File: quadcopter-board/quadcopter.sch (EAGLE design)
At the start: 75 parts, among them J2 AVR_SPI_PRG_6NS, SW1 PUSHBUTTON_SMD-VERTICAL-1, U2 ATMEGA128RFA1

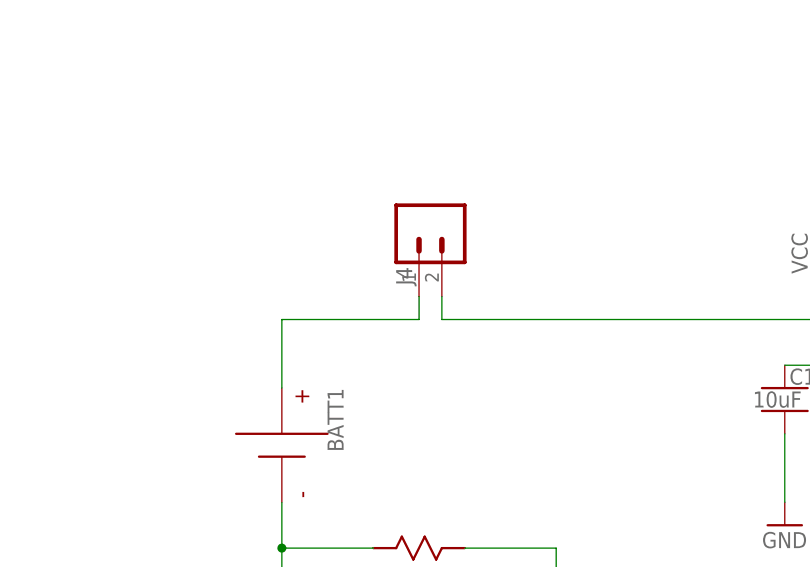
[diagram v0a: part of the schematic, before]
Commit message: Applied update to library and dru files. Passing DFM testing
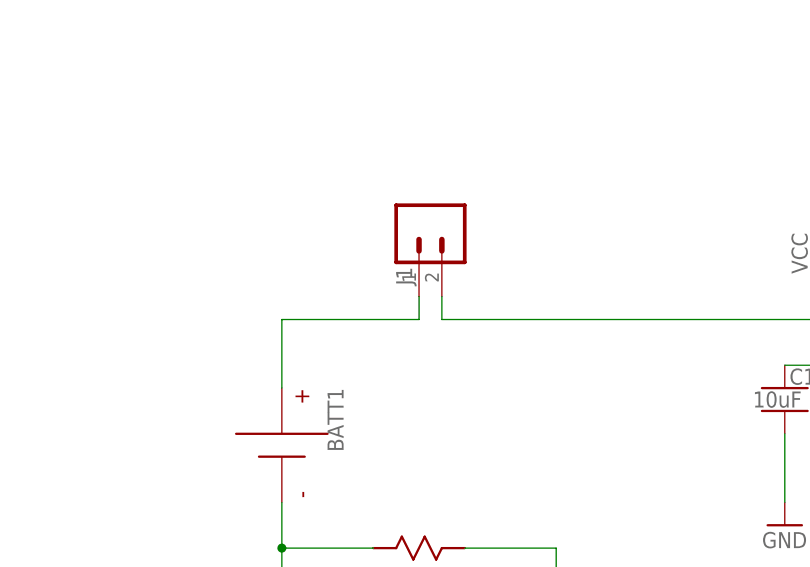
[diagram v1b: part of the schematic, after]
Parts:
- removed J4: (no value), quadparts:MALE_HEADER_2POS-2X1-0.1IN
- added J1: (no value), quadparts-rev2:MALE_HEADER_2POS-2X1-0.1IN
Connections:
- net N$17: now also J1.1; no longer J4.1
- net VCC: now also J1.2; no longer J4.2
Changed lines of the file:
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@@
 <setting verticaltext="up"/>
 </settings>
-<grid distance="0.1" unitdist="inch" unit="inch" style="lines" multiple="1" display="no" altdistance="0.01" altunitdist="inch" altunit="inch"/>
+<grid distance="0.05" unitdist="inch" unit="inch" style="lines" multiple="1" display="no" altdistance="0.01" altunitdist="inch" altunit="inch"/>
 <layers>
 <layer number="1" name="Top" color="4" fill="1" visible="no" active="no"/>
@@
 <part name="R1" library="quadparts_prebuilt" deviceset="RESISTOR_" device="SMD-2012-0805-10K" value="10K"/>
 <part name="R6" library="quadparts_prebuilt" deviceset="RESISTOR_" device="SMD-2012-0805-10K" value="10K"/>
-<part name="J4" library="quadparts" deviceset="MALE_HEADER_2POS" device="-2X1-0.1IN"/>
 <part name="GND36" library="SparkFun-Aesthetics" deviceset="GND" device=""/>
 <part name="GND37" library="SparkFun-Aesthetics" deviceset="GND" device=""/>
@@
 <part name="P+1" library="SparkFun-Aesthetics" deviceset="3.3V" device=""/>
 <part name="U$3" library="quadparts" deviceset="RESISTOR" device="" value="0"/>
+<part name="J1" library="quadparts-rev2" deviceset="MALE_HEADER_2POS" device="-2X1-0.1IN"/>
 </parts>
 <sheets>
@@
 <instance part="R1" gate="G$1" x="358.14" y="39.37"/>
 <instance part="R6" gate="G$1" x="358.14" y="31.75"/>
-<instance part="J4" gate="G$1" x="190.5" y="72.39" rot="R270"/>
 <instance part="GND36" gate="1" x="337.82" y="26.67"/>
 <instance part="GND37" gate="1" x="365.76" y="21.59"/>
@@
 <instance part="P+1" gate="G$1" x="410.21" y="133.35"/>
 <instance part="U$3" gate="G$1" x="190.5" y="34.29"/>
+<instance part="J1" gate="G$1" x="190.5" y="72.39" rot="R270"/>
 </instances>
 <busses>
@@
 <wire x1="259.08" y1="39.37" x2="259.08" y2="44.45" width="0.1524" layer="91"/>
 <junction x="238.76" y="54.61"/>
-<pinref part="J4" gate="G$1" pin="2"/>
 <wire x1="195.58" y1="62.23" x2="195.58" y2="59.69" width="0.1524" layer="91"/>
 <wire x1="195.58" y1="59.69" x2="238.76" y2="59.69" width="0.1524" layer="91"/>
@@
 <junction x="238.76" y="59.69"/>
 <pinref part="C1" gate="G$1" pin="1"/>
+<pinref part="J1" gate="G$1" pin="2"/>
 </segment>
 <segment>
@@
 <net name="N$17" class="0">
 <segment>
-<pinref part="J4" gate="G$1" pin="1"/>
 <wire x1="193.04" y1="62.23" x2="193.04" y2="59.69" width="0.1524" layer="91"/>
 <pinref part="BATT1" gate="G$1" pin="P"/>
 <wire x1="193.04" y1="59.69" x2="177.8" y2="59.69" width="0.1524" layer="91"/>
 <wire x1="177.8" y1="59.69" x2="177.8" y2="52.07" width="0.1524" layer="91"/>
-</segment>
-</net>
+<pinref part="J1" gate="G$1" pin="1"/>
+</segment>
+</net>
